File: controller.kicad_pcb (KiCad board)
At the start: 2 copper layers, 156.8 x 70.7 mm, 56 parts, among them J1 Conn_ST_STDC14, J2 USB_C_Receptacle_USB2.0_14P, SW1 SW_Push, SW10 SW_Push, SW11 SW_Push, SW12 SW_Push, SW13 SW_Push, SW2 SW_Push, SW3 SW_Push, SW4 SW_Push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

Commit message: pourin
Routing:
- net +3.3V: track 564.3 -> 601.0 mm, vias 9 -> 23
- net GND: track 347.0 -> 327.7 mm, vias 9 -> 16
- net RightTriggerBottom: track 67.8 -> 65.6 mm
- net LeftTriggerTop: track 82.7 -> 80.7 mm
- net DPadLeft: track 76.6 -> 78.1 mm
- net ButtonStart: track 41.8 -> 40.8 mm
- net LeftTriggerBottom: vias 1 -> 3
- added copper zone on B.Cu, net +3.3V
- added copper zone on F.Cu, net GND

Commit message: final commit before i do something really silly
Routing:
- net +3.3V: track 601.0 -> 592.0 mm
- net GND: track 327.7 -> 336.6 mm
- net LeftClick: track 63.5 -> 64.4 mm
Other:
- board text added: "1"
- board text added: "13"
- board text added: "14"
- board text added: "2"

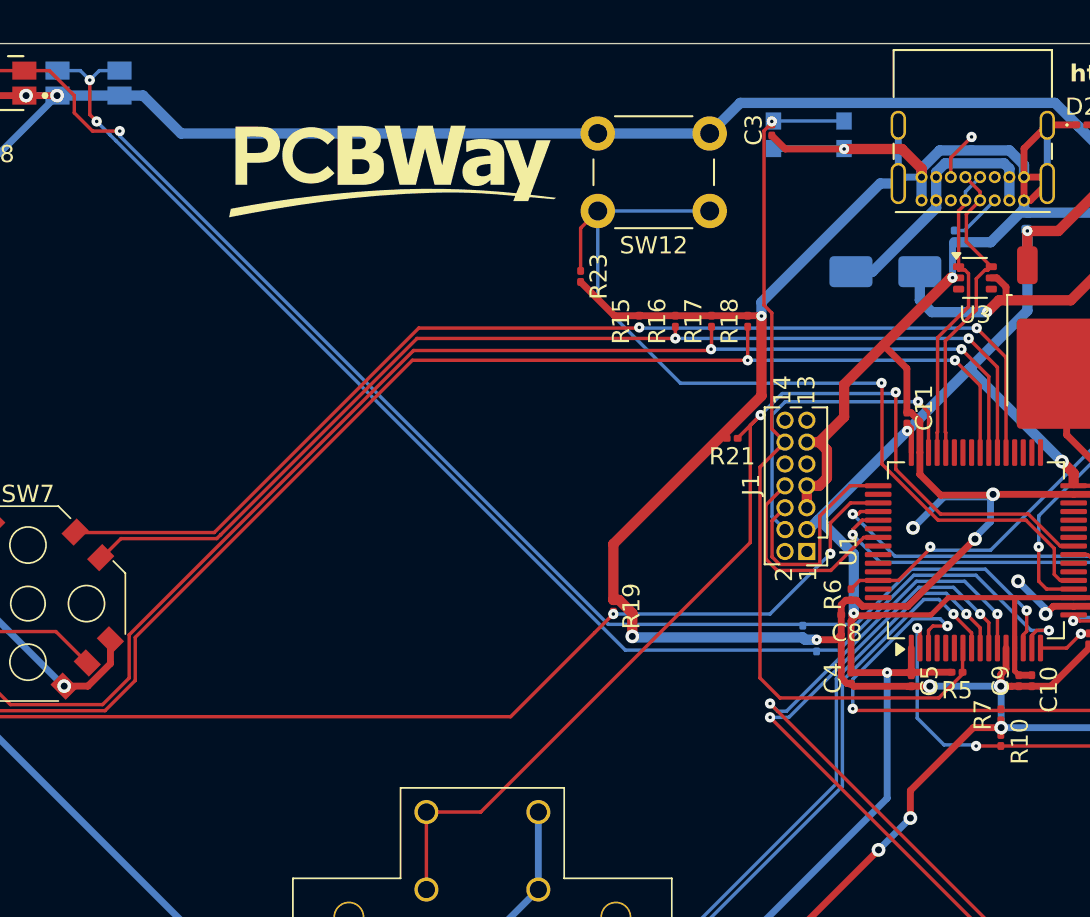
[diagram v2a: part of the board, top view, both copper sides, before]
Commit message: add 3220 component
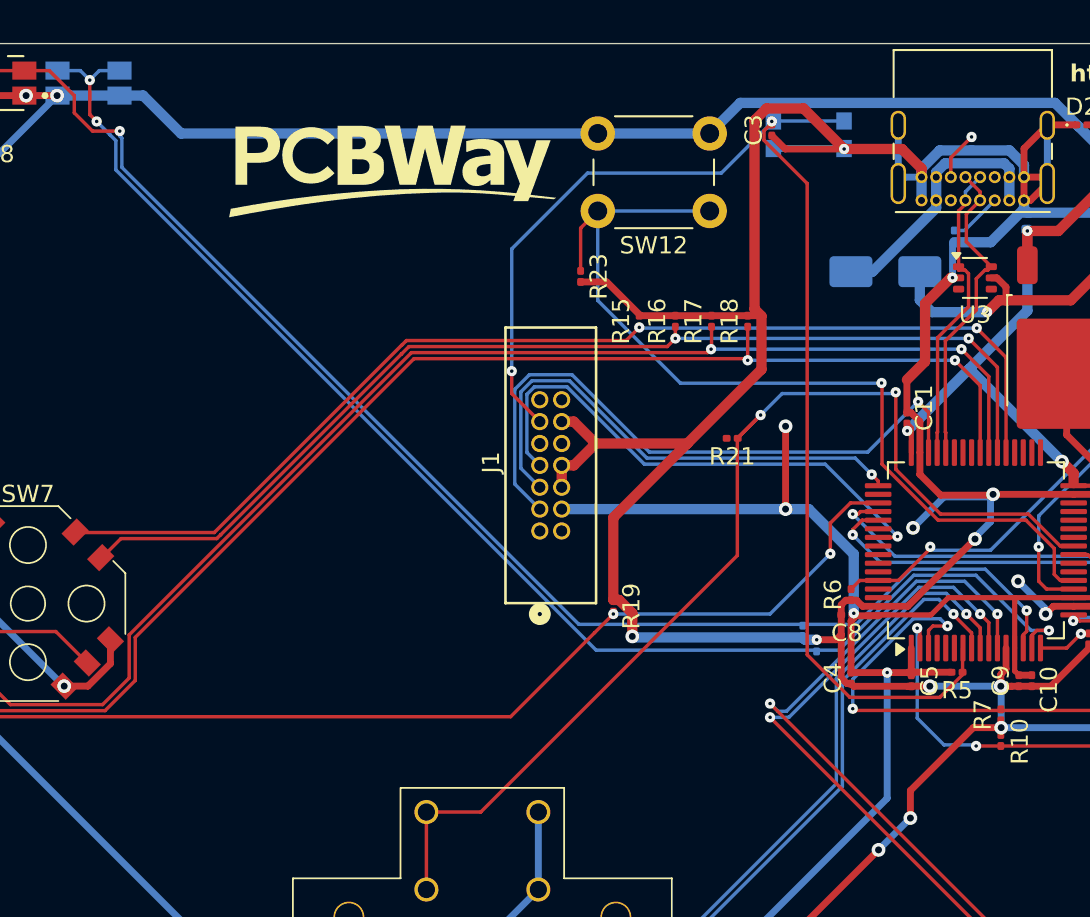
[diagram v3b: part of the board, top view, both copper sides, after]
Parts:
- J1: footprint Connector_PinHeader_1.27mm:PinHeader_2x07_P1.27mm_Vertical -> 3220_14_0100:CONN14_3220-14_CNC
- moved J1 14.3 mm to (113.4, 90.5), turned to 90 degrees
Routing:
- net nRST: track 52.0 -> 77.4 mm, vias 1 -> 2
- net SWDIO: track 19.0 -> 37.6 mm
- net SWO: track 12.3 -> 30.9 mm, vias 0 -> 1
- net SWCLK: track 13.0 -> 29.7 mm, vias 0 -> 1
- net +3.3V: track 592.0 -> 603.7 mm, vias 23 -> 25
- net GND: track 336.6 -> 340.6 mm, vias 16 -> 15
- net LeftTriggerTop: track 80.7 -> 81.7 mm
- net LeftTriggerBottom: track 79.7 -> 80.7 mm
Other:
- board text removed: "1"
- board text removed: "13"
- board text removed: "14"
- board text removed: "2"

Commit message: change some more tracks
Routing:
- net +3.3V: track 603.7 -> 601.9 mm
- net GND: track 340.6 -> 342.3 mm
- net ButtonUp: track 77.0 -> 78.1 mm
- net RightTriggerTop: track 72.4 -> 73.4 mm
- net ButtonRight: track 99.8 -> 100.5 mm
- net RightTriggerBottom: track 65.6 -> 66.3 mm

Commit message: tweak again
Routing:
- net GND: track 342.3 -> 337.4 mm, vias 15 -> 14
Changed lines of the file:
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@@
-	)
-	(via
-		(at 133.8 90.3)
-		(size 0.8)
-		(drill 0.4)
-		(layers "F.Cu" "B.Cu")
-		(net 2)
 	)
 	(via
@@
 	)
 	(segment
-		(start 138.3 88.5)
-		(end 135.6 88.5)
-		(width 0.4)
-		(layer "B.Cu")
-		(net 2)
-	)
-	(segment
 		(start 146.895125 72)
 		(end 140.466151 72)
@@
 	)
 	(segment
+		(start 138.45 88.3546)
+		(end 138.45 90.6)
+		(width 0.4)
+		(layer "B.Cu")
+		(net 2)
+	)
+	(segment
 		(start 117.5 96.6)
 		(end 117.52 96.62)
@@
 	)
 	(segment
+		(start 138.4477 88.3523)
+		(end 138.45 88.3546)
+		(width 0.4)
+		(layer "B.Cu")
+		(net 2)
+	)
+	(segment
 		(start 135.352265 68.382)
 		(end 134.295125 69.43914)
@@
 	)
 	(segment
-		(start 138.3 88.5)
-		(end 138.3 89.95)
-		(width 0.4)
-		(layer "B.Cu")
-		(net 2)
-	)
-	(segment
 		(start 140.245125 69.226952)
 		(end 139.400173 68.382)
@@
 	)
 	(segment
-		(start 138.4477 88.3523)
-		(end 138.3 88.5)
-		(width 0.4)
-		(layer "B.Cu")
-		(net 2)
-	)
-	(segment
 		(start 131.797 108.997)
 		(end 133.647 107.147)
@@
 	)
 	(segment
+		(start 138.102 90.948)
+		(end 137.4 90.948)
+		(width 0.4)
+		(layer "B.Cu")
+		(net 2)
+	)
+	(segment
 		(start 138.919 99.773425)
 		(end 139.201328 99.491097)
@@
 	)
 	(segment
+		(start 138.45 90.6)
+		(end 138.102 90.948)
+		(width 0.4)
+		(layer "B.Cu")
+		(net 2)
+	)
+	(segment
 		(start 134.295125 69.43914)
 		(end 134.295125 69.934)
@@
 	)
 	(segment
-		(start 138.3 89.95)
-		(end 137.4 90.85)
-		(width 0.4)
-		(layer "B.Cu")
-		(net 2)
-	)
-	(segment
 		(start 141.5 95.3)
 		(end 141.5 95)
@@
 	)
 	(segment
-		(start 135.6 88.5)
-		(end 133.8 90.3)
-		(width 0.4)
-		(layer "B.Cu")
-		(net 2)
-	)
-	(segment
 		(start 149.38 101.9)
 		(end 138.919 101.9)
@@
 	)
 	(segment
-		(start 137.4 90.85)
-		(end 137.4 90.948)
-		(width 0.4)
-		(layer "B.Cu")
-		(net 2)
-	)
-	(segment
 		(start 138.309099 73.715)
 		(end 136.195125 73.715)
@@
 	)
 	(segment
+		(start 186.2 84.1)
+		(end 168.4 84.1)
+		(width 0.2)
+		(layer "F.Cu")
+		(net 23)
+	)
+	(segment
+		(start 168.375 84.075)
+		(end 168 84.075)
+		(width 0.2)
+		(layer "F.Cu")
+		(net 23)
+	)
+	(segment
+		(start 130.6046 89.5)
+		(end 130.7523 89.3523)
+		(width 0.2)
+		(layer "F.Cu")
+		(net 23)
+	)
+	(segment
+		(start 168.4 84.1)
+		(end 168.3 84.1)
+		(width 0.2)
+		(layer "F.Cu")
+		(net 23)
+	)
+	(segment
+		(start 130.3 89.5)
+		(end 130.6046 89.5)
+		(width 0.2)
+		(layer "F.Cu")
+		(net 23)
+	)
+	(segment
+		(start 186.2 84.1)
+		(end 200.5 84.1)
+		(width 0.2)
+		(layer "F.Cu")
+		(net 23)
+	)
+	(segment
 		(start 130.7523 89.3523)
 		(end 131.776328 89.3523)
@@
 	)
 	(segment
-		(start 186.2 84.1)
-		(end 168.4 84.1)
-		(width 0.2)
-		(layer "F.Cu")
-		(net 23)
-	)
-	(segment
-		(start 168.375 84.075)
-		(end 168 84.075)
-		(width 0.2)
-		(layer "F.Cu")
-		(net 23)
-	)
-	(segment
-		(start 130.3 89.5)
-		(end 130.6046 89.5)
-		(width 0.2)
-		(layer "F.Cu")
-		(net 23)
-	)
-	(segment
-		(start 168.4 84.1)
-		(end 168.3 84.1)
-		(width 0.2)
-		(layer "F.Cu")
-		(net 23)
-	)
-	(segment
-		(start 130.6046 89.5)
-		(end 130.7523 89.3523)
-		(width 0.2)
-		(layer "F.Cu")
-		(net 23)
-	)
-	(segment
-		(start 186.2 84.1)
-		(end 200.5 84.1)
-		(width 0.2)
-		(layer "F.Cu")
-		(net 23)
-	)
-	(segment
 		(start 168 84.075)
 		(end 167.1 84.075)
@@
 	)
 	(segment
+		(start 133 92)
+		(end 132.8 92)
+		(width 0.2)
+		(layer "B.Cu")
+		(net 23)
+	)
+	(segment
+		(start 144.759223 91.998)
+		(end 133.002 91.998)
+		(width 0.2)
+		(layer "B.Cu")
+		(net 23)
+	)
+	(segment
+		(start 167.4 86.307224)
+		(end 162.060224 91.647)
+		(width 0.2)
+		(layer "B.Cu")
+		(net 23)
+	)
+	(segment
+		(start 132.8 92)
+		(end 130.3 89.5)
+		(width 0.2)
+		(layer "B.Cu")
+		(net 23)
+	)
+	(segment
+		(start 167.4 84.675)
+		(end 167.4 86.307224)
+		(width 0.2)
+		(layer "B.Cu")
+		(net 23)
+	)
+	(segment
+		(start 168 84.075)
+		(end 167.4 84.675)
+		(width 0.2)
+		(layer "B.Cu")
+		(net 23)
+	)
+	(segment
 		(start 145.110223 91.647)
 		(end 144.759223 91.998)
@@
 	)
 	(segment
-		(start 167.4 86.307224)
-		(end 162.060224 91.647)
-		(width 0.2)
-		(layer "B.Cu")
-		(net 23)
-	)
-	(segment
-		(start 168 84.075)
-		(end 167.4 84.675)
-		(width 0.2)
-		(layer "B.Cu")
-		(net 23)
-	)
-	(segment
-		(start 132.949 92.149)
-		(end 130.3 89.5)
+		(start 133.002 91.998)
+		(end 133 92)
 		(width 0.2)
 		(layer "B.Cu")
@@
 	)
 	(segment
-		(start 167.4 84.675)
-		(end 167.4 86.307224)
-		(width 0.2)
-		(layer "B.Cu")
-		(net 23)
-	)
-	(segment
-		(start 144.759223 91.998)
-		(end 133.409221 91.998)
-		(width 0.2)
-		(layer "B.Cu")
-		(net 23)
-	)
-	(segment
-		(start 133.258221 92.149)
-		(end 132.949 92.149)
-		(width 0.2)
-		(layer "B.Cu")
-		(net 23)
-	)
-	(segment
-		(start 133.409221 91.998)
-		(end 133.258221 92.149)
-		(width 0.2)
-		(layer "B.Cu")
-		(net 23)
-	)
-	(segment
 		(start 193.990448 85.2)
 		(end 168 85.2)
@@
 	)
 	(segment
-		(start 133.40361 92.5)
-		(end 133.55461 92.349)
-		(width 0.2)
-		(layer "B.Cu")
-		(net 25)
-	)
-	(segment
 		(start 130.3 90.7)
-		(end 132.1 92.5)
+		(end 131.949 92.349)
+		(width 0.2)
+		(layer "B.Cu")
+		(net 25)
+	)
+	(segment
+		(start 132.654612 92.351)
+		(end 133.145389 92.351)
 		(width 0.2)
 		(layer "B.Cu")
@@
 	)
 	(segment
-		(start 132.1 92.5)
-		(end 133.40361 92.5)
+		(start 133.145389 92.351)
+		(end 133.147389 92.349)
 		(width 0.2)
 		(layer "B.Cu")
@@
 	)
 	(segment
-		(start 133.55461 92.349)
-		(end 144.904612 92.349)
+		(start 132.652611 92.349)
+		(end 132.654612 92.351)
 		(width 0.2)
 		(layer "B.Cu")
@@
 		(width 0.2)
 		(layer "B.Cu")
+		(net 25)
+	)
+	(segment
+		(start 131.949 92.349)
+		(end 132.652611 92.349)
+		(width 0.2)
+		(layer "B.Cu")
+		(net 25)
+	)
+	(segment
+		(start 133.147389 92.349)
+		(end 144.904612 92.349)
+		(width 0.2)
+		(layer "B.Cu")
